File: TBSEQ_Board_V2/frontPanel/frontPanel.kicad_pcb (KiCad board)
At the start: 2 copper layers, 150 x 118 mm, 95 parts, among them J1 MJ-462, SW1 WAVE SELECT, U7 HT16K33_28SOP-A_

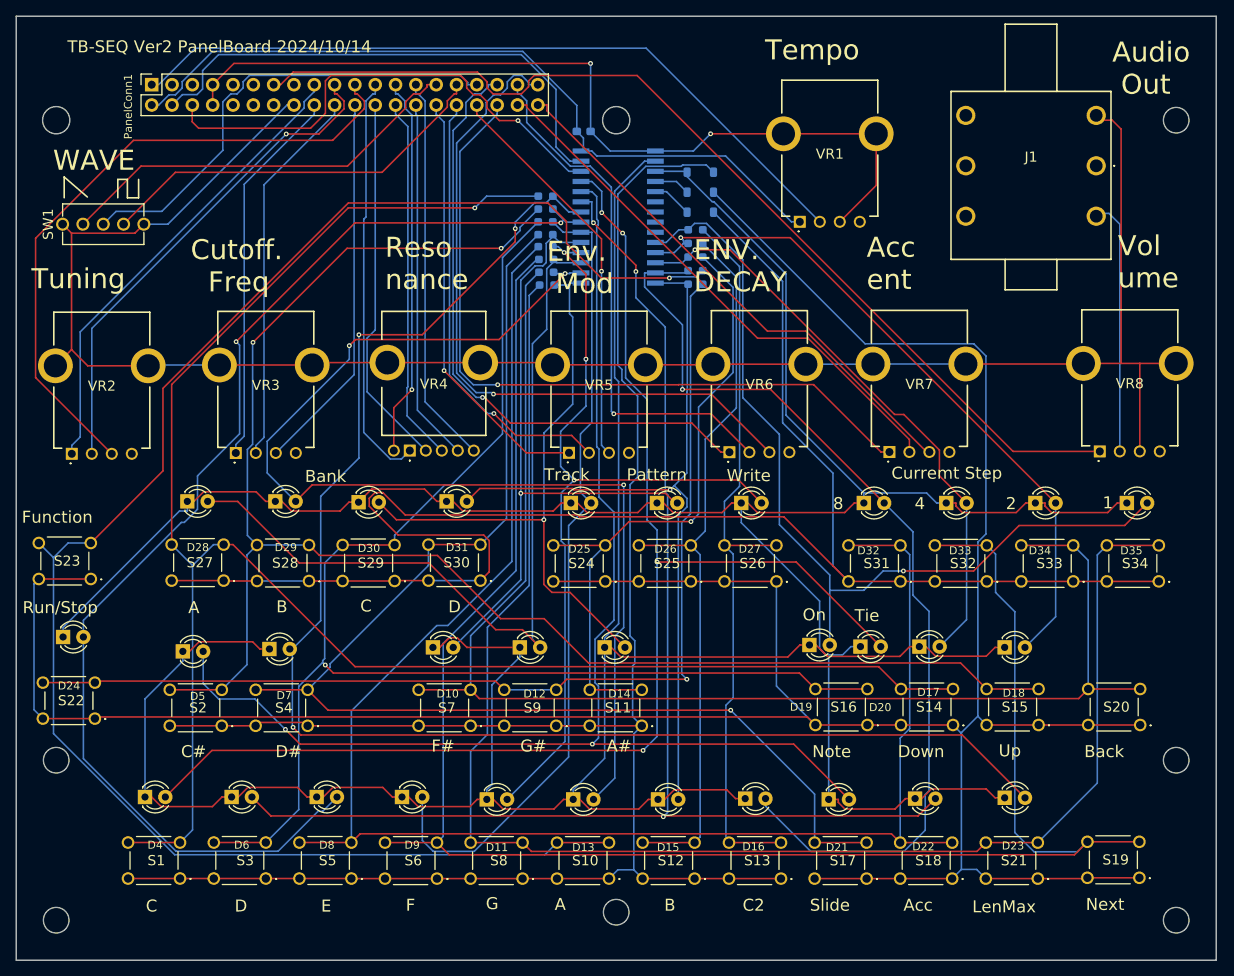
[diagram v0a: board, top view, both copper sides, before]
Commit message: mainBoard&FrontPanel
微修正
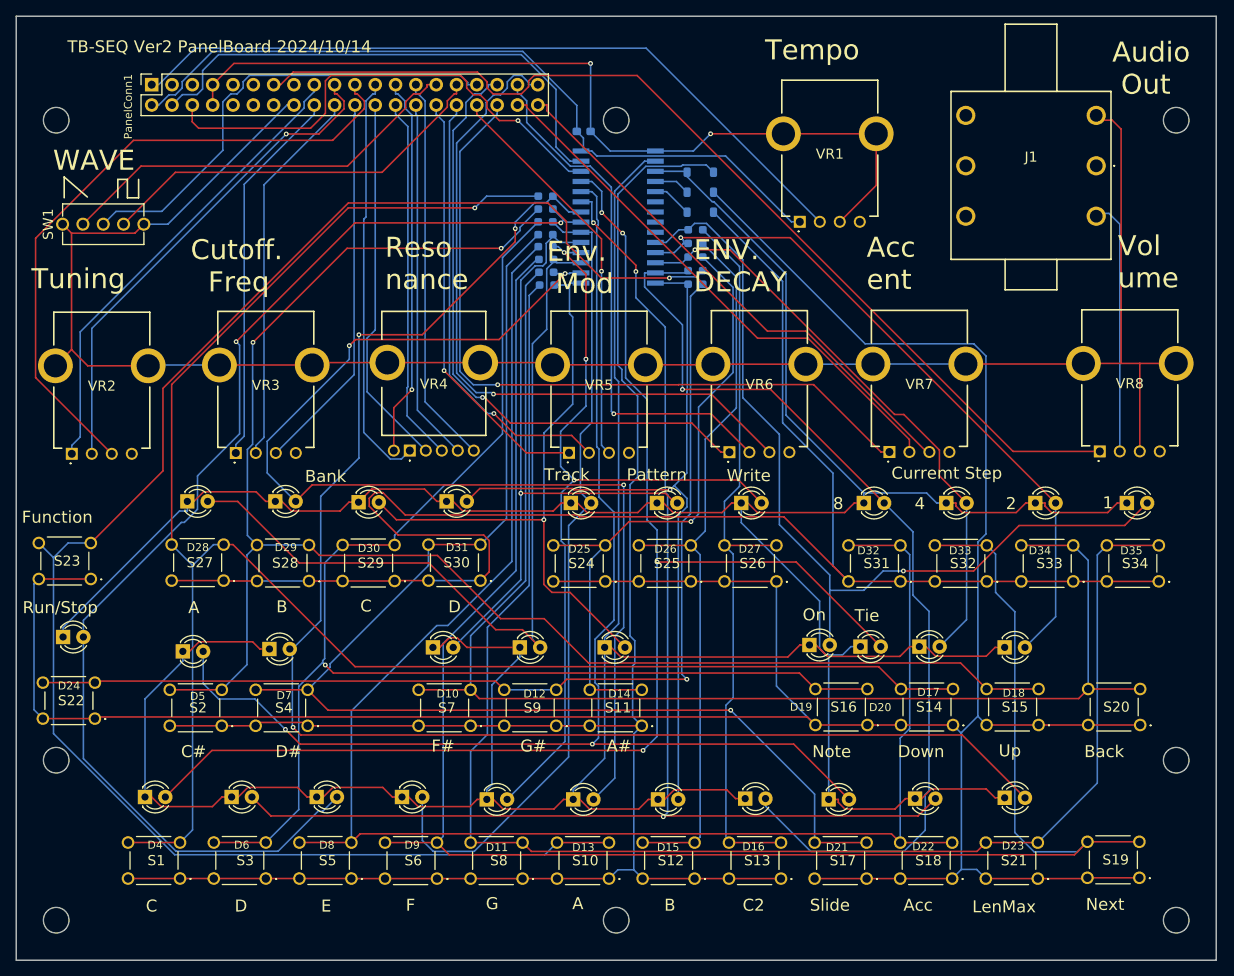
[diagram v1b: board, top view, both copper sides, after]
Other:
- outline, holes or cut-outs redrawn
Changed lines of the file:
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@@
 	(gr_circle
 		(center 95 33)
-		(end 96.7 33.1)
+		(end 96.6 33)
 		(stroke
 			(width 0.1)
@@
 	)
 	(gr_circle
-		(center 95 132)
-		(end 96.6 132)
+		(center 95 133)
+		(end 96.6 133)
 		(stroke
 			(width 0.1)
@@
 	(gr_circle
 		(center 25 33)
-		(end 26.7 33.1)
+		(end 26.6 33)
 		(stroke
 			(width 0.1)
@@
 	)
 	(gr_text "A"
-		(at 87.3 131.9 0)
+		(at 89.5 131.8 0)
 		(layer "F.SilkS")
 		(effects
@@
 			(polygon
 				(pts
-					(xy 89.282397 131.652327) (xy 89.258865 131.725339) (xy 89.192482 131.760571) (xy 89.181646 131.761137)
-					(xy 89.111616 131.736878) (xy 89.071721 131.674779) (xy 89.068073 131.652327) (xy 89.062753 131.553557)
-					(xy 89.056209 131.458431) (xy 89.048449 131.366918) (xy 89.039481 131.27899) (xy 89.029313 131.194617)
-					(xy 89.017953 131.113769) (xy 89.005411 131.036417) (xy 88.991692 130.962532) (xy 88.960762 130.825041)
-					(xy 88.925228 130.701062) (xy 88.885155 130.590358) (xy 88.840607 130.492692) (xy 88.79165 130.40783)
-					(xy 88.738349 130.335533) (xy 88.680769 130.275568) (xy 88.618974 130.227696) (xy 88.553029 130.191683)
-					(xy 88.483 130.167292) (xy 88.408952 130.154287) (xy 88.330949 130.152431) (xy 88.238477 130.166562)
-					(xy 88.153346 130.201875) (xy 88.075268 130.256717) (xy 88.003951 130.329435) (xy 87.939107 130.418374)
-					(xy 87.89933 130.485862) (xy 87.862215 130.559334) (xy 87.827676 130.638301) (xy 87.795627 130.722273)
-					(xy 87.765982 130.81076) (xy 87.738656 130.903271) (xy 87.713562 130.999317) (xy 87.690615 131.098408)
-					(xy 87.679919 131.148942) (xy 87.762813 131.128747) (xy 87.850447 131.111573) (xy 87.942366 131.097617)
-					(xy 88.038112 131.08708) (xy 88.137229 131.08016) (xy 88.239262 131.077057) (xy 88.343753 131.077971)
-					(xy 88.450246 131.0831) (xy 88.558285 131.092643) (xy 88.667412 131.106801) (xy 88.740544 131.1189)
-					(xy 88.802227 131.160731) (xy 88.816697 131.234454) (xy 88.814183 131.24493) (xy 88.769 131.308171)
-					(xy 88.694415 131.32737) (xy 88.683757 131.325896) (xy 88.604637 131.312618) (xy 88.517104 131.301938)
-					(xy 88.422713 131.294307) (xy 88.323021 131.29018) (xy 88.219583 131.290008) (xy 88.113955 131.294245)
-					(xy 88.007694 131.303344) (xy 87.902354 131.317756) (xy 87.799492 131.337936) (xy 87.700664 131.364335)
-					(xy 87.637787 131.385614) (xy 87.627318 131.459958) (xy 87.617093 131.535003) (xy 87.607357 131.610407)
-					(xy 87.60225 131.652327) (xy 87.571474 131.722297) (xy 87.506906 131.759001) (xy 87.484647 131.761137)
-					(xy 87.415224 131.732738) (xy 87.387339 131.66339) (xy 87.387927 131.652327) (xy 87.398643 131.539661)
-					(xy 87.411045 131.431273) (xy 87.425081 131.327117) (xy 87.440703 131.227144) (xy 87.457861 131.131308)
-					(xy 87.476506 131.039561) (xy 87.496587 130.951857) (xy 87.518055 130.868147) (xy 87.54086 130.788385)
-					(xy 87.564953 130.712524) (xy 87.590285 130.640516) (xy 87.644463 130.50787) (xy 87.702998 130.390071)
-					(xy 87.765492 130.286741) (xy 87.831549 130.197501) (xy 87.900771 130.121974) (xy 87.972761 130.059782)
-					(xy 88.047122 130.010548) (xy 88.123457 129.973893) (xy 88.201369 129.94944) (xy 88.28046 129.93681)
-					(xy 88.320324 129.934811) (xy 88.425402 129.935927) (xy 88.524762 129.94918) (xy 88.618346 129.975006)
-					(xy 88.706094 130.013837) (xy 88.787947 130.066109) (xy 88.863847 130.132255) (xy 88.933734 130.21271)
-					(xy 88.997548 130.307907) (xy 89.055232 130.418282) (xy 89.106726 130.544267) (xy 89.151971 130.686298)
-					(xy 89.172232 130.763466) (xy 89.190909 130.844808) (xy 89.207993 130.930379) (xy 89.223479 131.020232)
-					(xy 89.237358 131.114422) (xy 89.249623 131.213004) (xy 89.260267 131.316031) (xy 89.269282 131.423557)
-					(xy 89.276661 131.535638)
+					(xy 91.482397 131.552327) (xy 91.458865 131.625339) (xy 91.392482 131.660571) (xy 91.381646 131.661137)
+					(xy 91.311616 131.636878) (xy 91.271721 131.574779) (xy 91.268073 131.552327) (xy 91.262753 131.453557)
+					(xy 91.256209 131.358431) (xy 91.248449 131.266918) (xy 91.239481 131.17899) (xy 91.229313 131.094617)
+					(xy 91.217953 131.013769) (xy 91.205411 130.936417) (xy 91.191692 130.862532) (xy 91.160762 130.725041)
+					(xy 91.125228 130.601062) (xy 91.085155 130.490358) (xy 91.040607 130.392692) (xy 90.99165 130.30783)
+					(xy 90.938349 130.235533) (xy 90.880769 130.175568) (xy 90.818974 130.127696) (xy 90.753029 130.091683)
+					(xy 90.683 130.067292) (xy 90.608952 130.054287) (xy 90.530949 130.052431) (xy 90.438477 130.066562)
+					(xy 90.353346 130.101875) (xy 90.275268 130.156717) (xy 90.203951 130.229435) (xy 90.139107 130.318374)
+					(xy 90.09933 130.385862) (xy 90.062215 130.459334) (xy 90.027676 130.538301) (xy 89.995627 130.622273)
+					(xy 89.965982 130.71076) (xy 89.938656 130.803271) (xy 89.913562 130.899317) (xy 89.890615 130.998408)
+					(xy 89.879919 131.048942) (xy 89.962813 131.028747) (xy 90.050447 131.011573) (xy 90.142366 130.997617)
+					(xy 90.238112 130.98708) (xy 90.337229 130.98016) (xy 90.439262 130.977057) (xy 90.543753 130.977971)
+					(xy 90.650246 130.9831) (xy 90.758285 130.992643) (xy 90.867412 131.006801) (xy 90.940544 131.0189)
+					(xy 91.002227 131.060731) (xy 91.016697 131.134454) (xy 91.014183 131.14493) (xy 90.969 131.208171)
+					(xy 90.894415 131.22737) (xy 90.883757 131.225896) (xy 90.804637 131.212618) (xy 90.717104 131.201938)
+					(xy 90.622713 131.194307) (xy 90.523021 131.19018) (xy 90.419583 131.190008) (xy 90.313955 131.194245)
+					(xy 90.207694 131.203344) (xy 90.102354 131.217756) (xy 89.999492 131.237936) (xy 89.900664 131.264335)
+					(xy 89.837787 131.285614) (xy 89.827318 131.359958) (xy 89.817093 131.435003) (xy 89.807357 131.510407)
+					(xy 89.80225 131.552327) (xy 89.771474 131.622297) (xy 89.706906 131.659001) (xy 89.684647 131.661137)
+					(xy 89.615224 131.632738) (xy 89.587339 131.56339) (xy 89.587927 131.552327) (xy 89.598643 131.439661)
+					(xy 89.611045 131.331273) (xy 89.625081 131.227117) (xy 89.640703 131.127144) (xy 89.657861 131.031308)
+					(xy 89.676506 130.939561) (xy 89.696587 130.851857) (xy 89.718055 130.768147) (xy 89.74086 130.688385)
+					(xy 89.764953 130.612524) (xy 89.790285 130.540516) (xy 89.844463 130.40787) (xy 89.902998 130.290071)
+					(xy 89.965492 130.186741) (xy 90.031549 130.097501) (xy 90.100771 130.021974) (xy 90.172761 129.959782)
+					(xy 90.247122 129.910548) (xy 90.323457 129.873893) (xy 90.401369 129.84944) (xy 90.48046 129.83681)
+					(xy 90.520324 129.834811) (xy 90.625402 129.835927) (xy 90.724762 129.84918) (xy 90.818346 129.875006)
+					(xy 90.906094 129.913837) (xy 90.987947 129.966109) (xy 91.063847 130.032255) (xy 91.133734 130.11271)
+					(xy 91.197548 130.207907) (xy 91.255232 130.318282) (xy 91.306726 130.444267) (xy 91.351971 130.586298)
+					(xy 91.372232 130.663466) (xy 91.390909 130.744808) (xy 91.407993 130.830379) (xy 91.423479 130.920232)
+					(xy 91.437358 131.014422) (xy 91.449623 131.113004) (xy 91.460267 131.216031) (xy 91.469282 131.323557)
+					(xy 91.476661 131.435638)
 				)
 			)
